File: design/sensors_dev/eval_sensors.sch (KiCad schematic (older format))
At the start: 32 parts, among them J4 Conn_01x12, U2 BMC150, U3 LSM6DS3HTR, U4 FXAS21002, U5 MS5607-02BA03, U6 LIS3DHTR

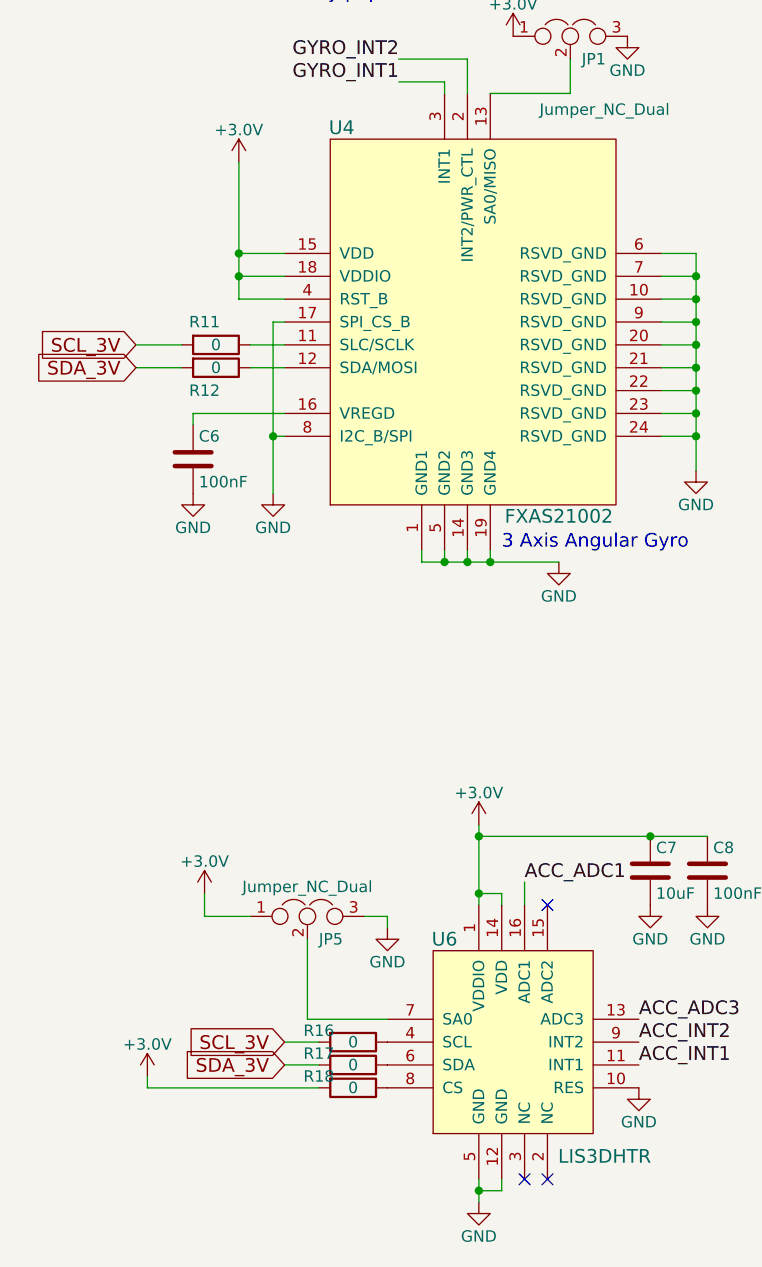
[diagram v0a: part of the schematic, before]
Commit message: fix FXAS21002 protocol and bidir mosfets
- Per review, tie pin 17 of FXAS21002 to HIGH the way it should be for
  I2C mode.
- switch out bidirectional mosfets for some that would actually work.
  (VGS_th too hih relative to VDS for the old ones)
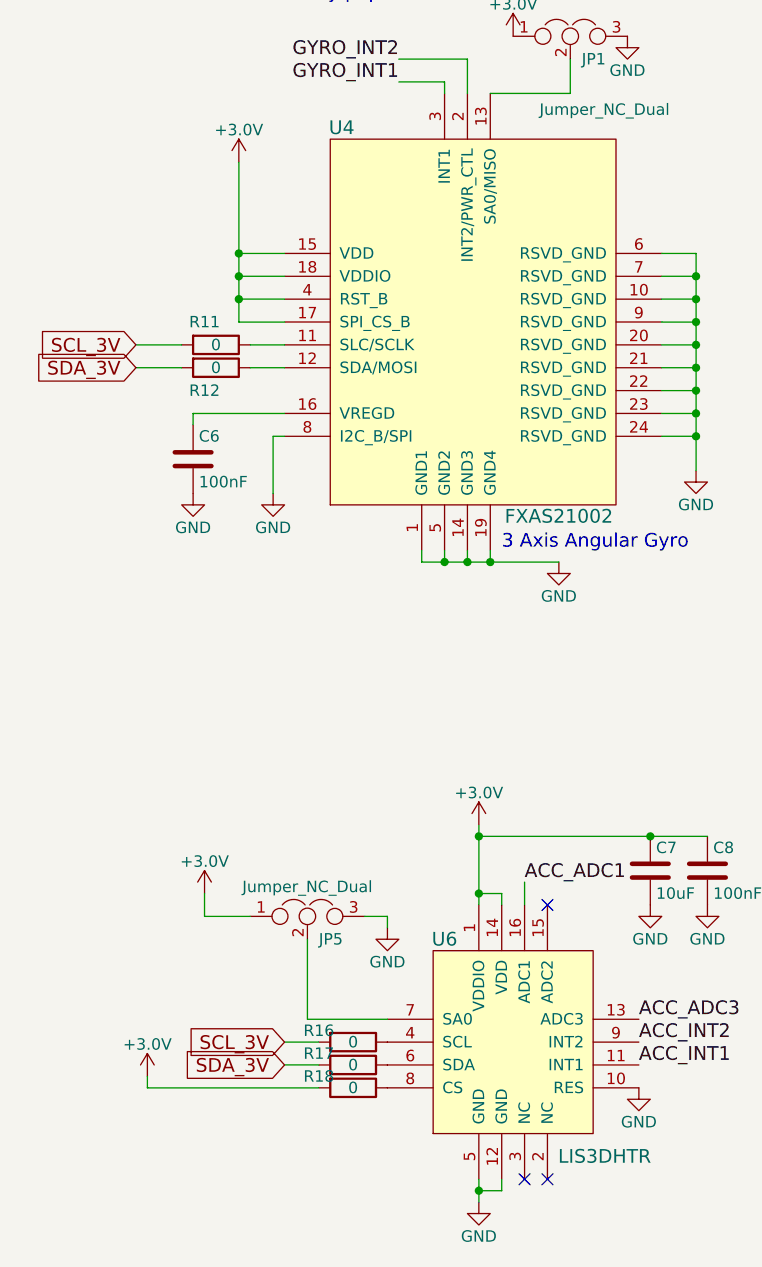
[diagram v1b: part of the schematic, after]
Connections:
- net +3.0V: now also U4.17 (SPI_CS_B)
- net GND: no longer U4.17 (SPI_CS_B)
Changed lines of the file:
@@
 	1950 6000 2100 6000
 Wire Wire Line
-	2800 6700 2800 6600
+	2800 6600 2800 6700
 Wire Wire Line
 	2900 6600 2900 6650
@@
 Connection ~ 2850 3900
 Wire Wire Line
-	1900 2850 1900 3600
-Wire Wire Line
-	1900 3350 1950 3350
-Wire Wire Line
 	1550 3300 1550 3250
 Wire Wire Line
 	1550 3250 1950 3250
 Wire Wire Line
-	1750 2150 1750 2750
+	1750 2150 1750 2850
 Wire Wire Line
 	1750 2550 1950 2550
@@
 	1500 3050 1300 3050
 Wire Wire Line
-	1950 2850 1900 2850
-Connection ~ 1900 3350
+	1750 2850 1950 2850
 Wire Wire Line
 	2450 1800 2650 1800
@@
 Wire Wire Line
 	2400 5450 2300 5450
+Wire Wire Line
+	1900 3600 1900 3350
+Wire Wire Line
+	1900 3350 1950 3350
+Connection ~ 1750 2750
 $EndSCHEMATC
